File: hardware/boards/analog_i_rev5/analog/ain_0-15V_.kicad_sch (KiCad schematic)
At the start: 3 parts, among them IC22001 INA826AIDR

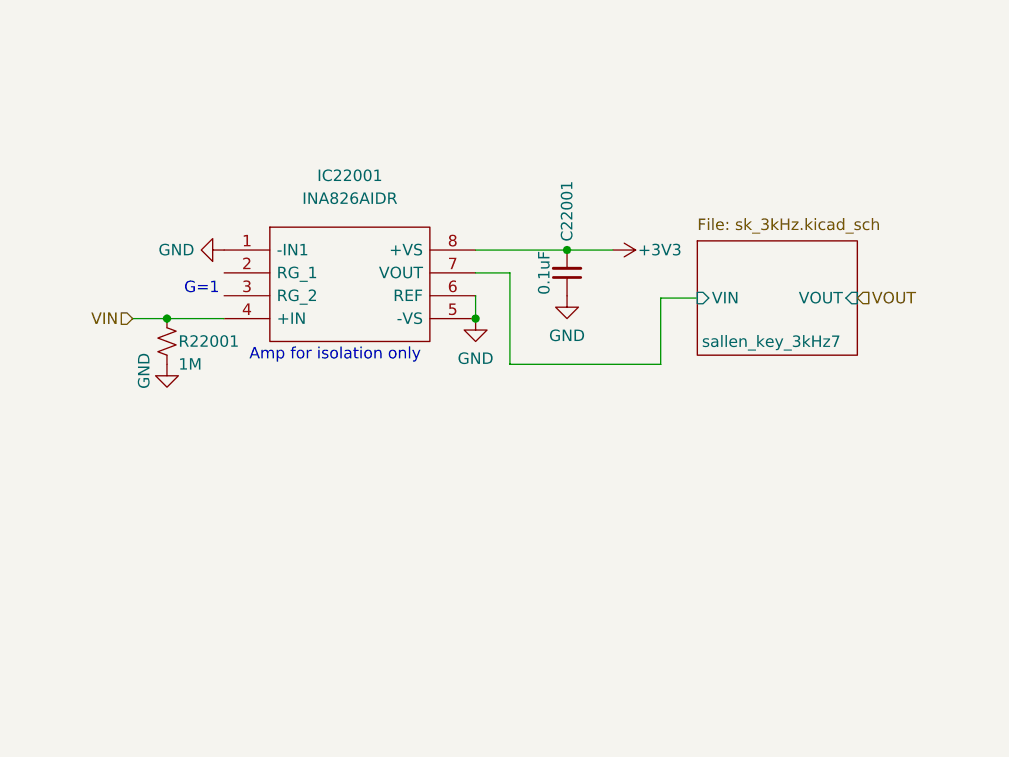
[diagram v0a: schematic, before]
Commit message: add 24V user power. make two voltage inputs 0-15V.
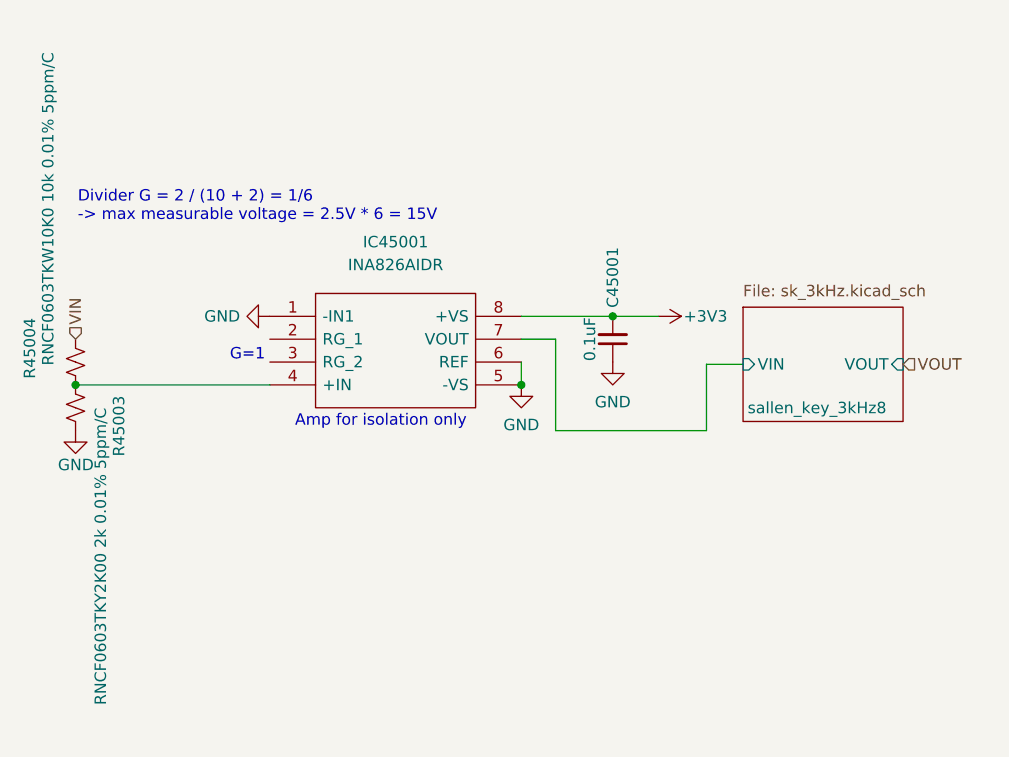
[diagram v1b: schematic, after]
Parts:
- removed C22001: 0.1uF, Capacitor_SMD:C_0402_1005Metric, symbol Device:C_Small
- removed IC22001: INA826AIDR, aaa:SOIC127P600X175-8N, symbol aaa:INA826AIDR
- removed R22001: 1M, Resistor_SMD:R_0402_1005Metric, symbol Device:R_Small_US
- added C45001: 0.1uF, Capacitor_SMD:C_0402_1005Metric, symbol Device:C_Small
- added IC45001: INA826AIDR, aaa:SOIC127P600X175-8N, symbol aaa:INA826AIDR
- added R45003: RNCF0603TKY2K00 2k 0.01% 5ppm/C, Resistor_SMD:R_0603_1608Metric, symbol Device:R_Small_US
- added R45004: RNCF0603TKW10K0 10k 0.01% 5ppm/C, Resistor_SMD:R_0603_1608Metric, symbol Device:R_Small_US
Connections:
- net +3V3: now also C45001.2, IC45001.8 (+VS)
- net GND: now also C45001.1, IC45001.1 (-IN1), IC45001.5 (-VS), IC45001.6 (REF), R45003.2
- net VIN: now also R45004.2
- new net: IC45001.4 (+IN), R45003.1, R45004.1
- new net sallen_key_3kHz8/VIN: IC45001.7 (VOUT)
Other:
- removed sheet sallen_key_3kHz7
- added sheet sallen_key_3kHz8 (sk_3kHz.kicad_sch)
- note added: "Divider G = 2 / (10 + 2) = 1/6 -> max measurable voltage = 2.5V * 6 = 15V"

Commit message: remove redundant esd diodes
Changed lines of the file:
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@@
 	(wire
 		(pts
-			(xy 155.448 109.728) (xy 138.684 109.728)
+			(xy 138.684 109.728) (xy 155.448 109.728)
 		)
 		(stroke

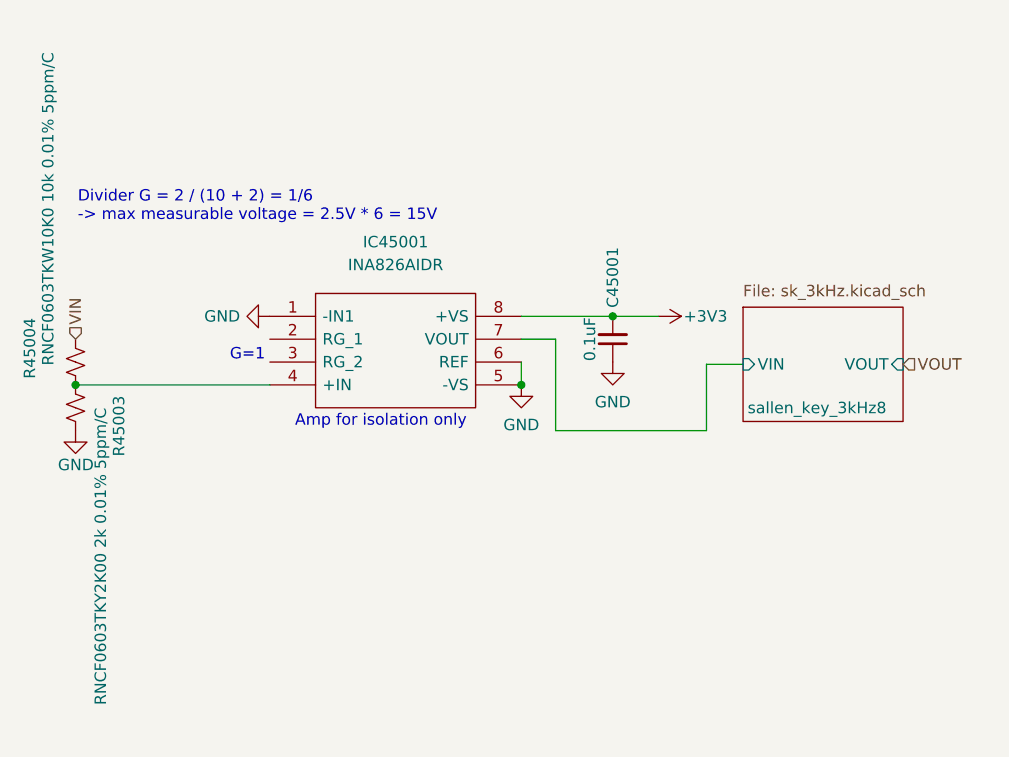
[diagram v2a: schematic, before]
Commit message: do layout for voltage inputs and dac/pwm outputs
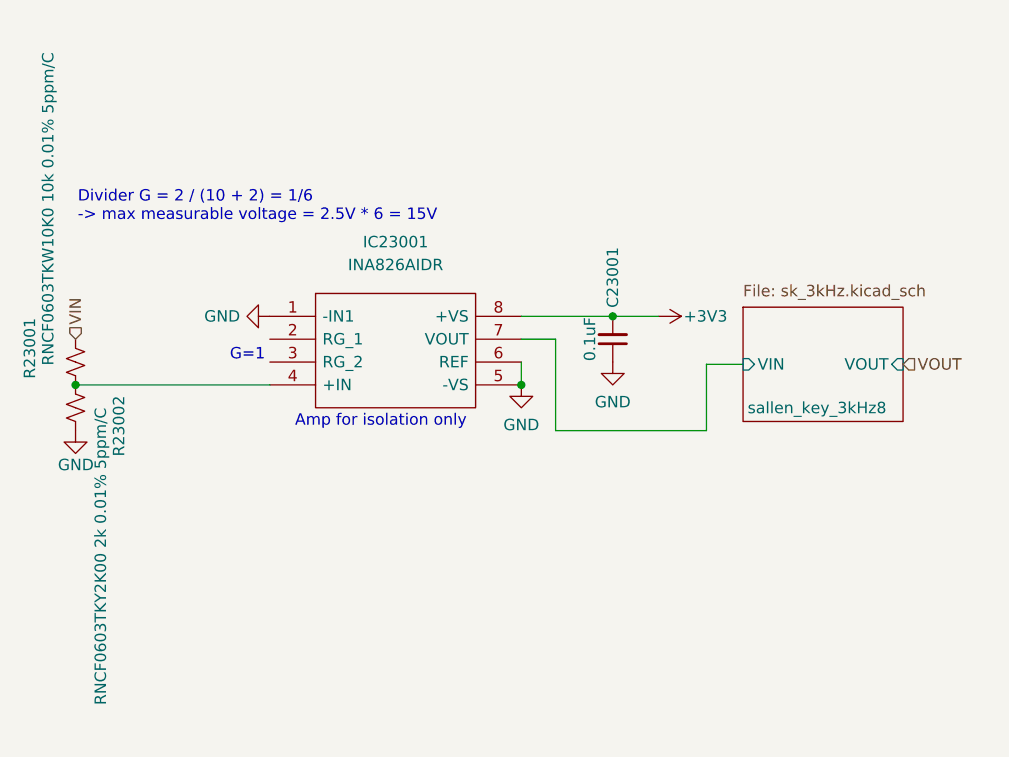
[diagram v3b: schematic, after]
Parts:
- renumbered C45001 to C23001, IC45001 to IC23001, R45004 to R23001, R45003 to R23002
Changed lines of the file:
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@@
 		(dnp no)
 		(fields_autoplaced yes)
-		(property "Reference" "IC45001"
+		(property "Reference" "IC23001"
 			(at 120.904 88.773 0)
 			(effects
@@
 		(on_board yes)
 		(dnp no)
-		(property "Reference" "R45003"
+		(property "Reference" "R23002"
 			(at 90.17 109.22 90)
 			(effects
@@
 		(on_board yes)
 		(dnp no)
-		(property "Reference" "#PWR45009"
+		(property "Reference" "#PWR23001"
 			(at 85.344 116.078 0)
 			(effects
@@
 		(on_board yes)
 		(dnp no)
-		(property "Reference" "#PWR45008"
+		(property "Reference" "#PWR23005"
 			(at 146.304 97.028 0)
 			(effects
@@
 		(on_board yes)
 		(dnp no)
-		(property "Reference" "R45004"
+		(property "Reference" "R23001"
 			(at 80.264 100.584 90)
 			(effects
@@
 		(dnp no)
 		(fields_autoplaced yes)
-		(property "Reference" "#PWR45005"
+		(property "Reference" "#PWR23002"
 			(at 100.584 97.028 0)
 			(effects
@@
 		(dnp no)
 		(fields_autoplaced yes)
-		(property "Reference" "#PWR45006"
+		(property "Reference" "#PWR23003"
 			(at 134.874 110.998 0)
 			(effects
@@
 		(on_board yes)
 		(dnp no)
-		(property "Reference" "C45001"
+		(property "Reference" "C23001"
 			(at 145.034 92.71 90)
 			(effects
@@
 		(dnp no)
 		(fields_autoplaced yes)
-		(property "Reference" "#PWR45007"
+		(property "Reference" "#PWR23004"
 			(at 145.034 108.458 0)
 			(effects

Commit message: shorten board and update combined layout
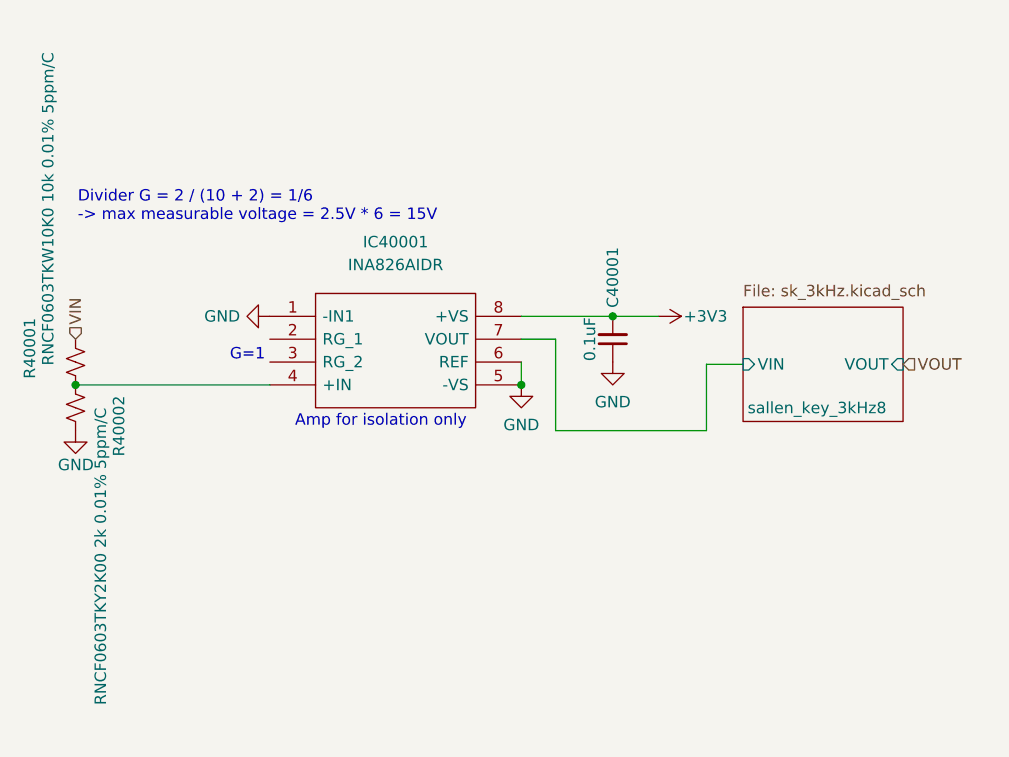
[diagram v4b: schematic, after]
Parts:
- renumbered C23001 to C40001, IC23001 to IC40001, R23001 to R40001, R23002 to R40002
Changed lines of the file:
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@@
 		(dnp no)
 		(fields_autoplaced yes)
-		(property "Reference" "IC23001"
+		(property "Reference" "IC40001"
 			(at 120.904 88.773 0)
 			(effects
@@
 		)
 		(instances
+			(project "analog_i"
+				(path "/5a60c4b1-b6cb-416e-8883-8291fa089b87/c2baf18d-2b19-4edb-98b3-535275ee271f/be220027-a1e7-4f8a-b4af-8d208623fd51"
+					(reference "IC40001")
+					(unit 1)
+				)
+				(path "/5a60c4b1-b6cb-416e-8883-8291fa089b87/c2baf18d-2b19-4edb-98b3-535275ee271f/ed2f7b43-1244-451f-9def-7c9639b384e1"
+					(reference "IC42001")
+					(unit 1)
+				)
+			)
 			(project "analog_frontend_panel"
 				(path "/c241d083-1323-4b4a-a540-956d0afb7b72/be220027-a1e7-4f8a-b4af-8d208623fd51"
@@
 		(on_board yes)
 		(dnp no)
-		(property "Reference" "R23002"
+		(property "Reference" "R40002"
 			(at 90.17 109.22 90)
 			(effects
@@
 		)
 		(instances
+			(project "analog_i"
+				(path "/5a60c4b1-b6cb-416e-8883-8291fa089b87/c2baf18d-2b19-4edb-98b3-535275ee271f/be220027-a1e7-4f8a-b4af-8d208623fd51"
+					(reference "R40002")
+					(unit 1)
+				)
+				(path "/5a60c4b1-b6cb-416e-8883-8291fa089b87/c2baf18d-2b19-4edb-98b3-535275ee271f/ed2f7b43-1244-451f-9def-7c9639b384e1"
+					(reference "R42002")
+					(unit 1)
+				)
+			)
 			(project "analog_frontend_panel"
 				(path "/c241d083-1323-4b4a-a540-956d0afb7b72/be220027-a1e7-4f8a-b4af-8d208623fd51"
@@
 		(on_board yes)
 		(dnp no)
-		(property "Reference" "#PWR23001"
+		(property "Reference" "#PWR231"
 			(at 85.344 116.078 0)
 			(effects
@@
 		)
 		(instances
+			(project "analog_i"
+				(path "/5a60c4b1-b6cb-416e-8883-8291fa089b87/c2baf18d-2b19-4edb-98b3-535275ee271f/be220027-a1e7-4f8a-b4af-8d208623fd51"
+					(reference "#PWR231")
+					(unit 1)
+				)
+				(path "/5a60c4b1-b6cb-416e-8883-8291fa089b87/c2baf18d-2b19-4edb-98b3-535275ee271f/ed2f7b43-1244-451f-9def-7c9639b384e1"
+					(reference "#PWR240")
+					(unit 1)
+				)
+			)
 			(project "analog_frontend_panel"
 				(path "/c241d083-1323-4b4a-a540-956d0afb7b72/be220027-a1e7-4f8a-b4af-8d208623fd51"
@@
 		(on_board yes)
 		(dnp no)
-		(property "Reference" "#PWR23005"
+		(property "Reference" "#PWR229"
 			(at 146.304 97.028 0)
 			(effects
@@
 		)
 		(instances
+			(project "analog_i"
+				(path "/5a60c4b1-b6cb-416e-8883-8291fa089b87/c2baf18d-2b19-4edb-98b3-535275ee271f/be220027-a1e7-4f8a-b4af-8d208623fd51"
+					(reference "#PWR229")
+					(unit 1)
+				)
+				(path "/5a60c4b1-b6cb-416e-8883-8291fa089b87/c2baf18d-2b19-4edb-98b3-535275ee271f/ed2f7b43-1244-451f-9def-7c9639b384e1"
+					(reference "#PWR238")
+					(unit 1)
+				)
+			)
 			(project "analog_frontend_panel"
 				(path "/c241d083-1323-4b4a-a540-956d0afb7b72/be220027-a1e7-4f8a-b4af-8d208623fd51"
@@
 		(on_board yes)
 		(dnp no)
-		(property "Reference" "R23001"
+		(property "Reference" "R40001"
 			(at 80.264 100.584 90)
 			(effects
@@
 		)
 		(instances
+			(project "analog_i"
+				(path "/5a60c4b1-b6cb-416e-8883-8291fa089b87/c2baf18d-2b19-4edb-98b3-535275ee271f/be220027-a1e7-4f8a-b4af-8d208623fd51"
+					(reference "R40001")
+					(unit 1)
+				)
+				(path "/5a60c4b1-b6cb-416e-8883-8291fa089b87/c2baf18d-2b19-4edb-98b3-535275ee271f/ed2f7b43-1244-451f-9def-7c9639b384e1"
+					(reference "R42001")
+					(unit 1)
+				)
+			)
 			(project "analog_frontend_panel"
 				(path "/c241d083-1323-4b4a-a540-956d0afb7b72/be220027-a1e7-4f8a-b4af-8d208623fd51"
@@
 		(dnp no)
 		(fields_autoplaced yes)
-		(property "Reference" "#PWR23002"
+		(property "Reference" "#PWR230"
 			(at 100.584 97.028 0)
 			(effects
@@
 		)
 		(instances
+			(project "analog_i"
+				(path "/5a60c4b1-b6cb-416e-8883-8291fa089b87/c2baf18d-2b19-4edb-98b3-535275ee271f/be220027-a1e7-4f8a-b4af-8d208623fd51"
+					(reference "#PWR230")
+					(unit 1)
+				)
+				(path "/5a60c4b1-b6cb-416e-8883-8291fa089b87/c2baf18d-2b19-4edb-98b3-535275ee271f/ed2f7b43-1244-451f-9def-7c9639b384e1"
+					(reference "#PWR239")
+					(unit 1)
+				)
+			)
 			(project "analog_frontend_panel"
 				(path "/c241d083-1323-4b4a-a540-956d0afb7b72/be220027-a1e7-4f8a-b4af-8d208623fd51"
@@
 		(dnp no)
 		(fields_autoplaced yes)
-		(property "Reference" "#PWR23003"
+		(property "Reference" "#PWR227"
 			(at 134.874 110.998 0)
 			(effects
@@
 		)
 		(instances
+			(project "analog_i"
+				(path "/5a60c4b1-b6cb-416e-8883-8291fa089b87/c2baf18d-2b19-4edb-98b3-535275ee271f/be220027-a1e7-4f8a-b4af-8d208623fd51"
+					(reference "#PWR227")
+					(unit 1)
+				)
+				(path "/5a60c4b1-b6cb-416e-8883-8291fa089b87/c2baf18d-2b19-4edb-98b3-535275ee271f/ed2f7b43-1244-451f-9def-7c9639b384e1"
+					(reference "#PWR236")
+					(unit 1)
+				)
+			)
 			(project "analog_frontend_panel"
 				(path "/c241d083-1323-4b4a-a540-956d0afb7b72/be220027-a1e7-4f8a-b4af-8d208623fd51"
@@
 		(on_board yes)
 		(dnp no)
-		(property "Reference" "C23001"
+		(property "Reference" "C40001"
 			(at 145.034 92.71 90)
 			(effects
@@
 		)
 		(instances
+			(project "analog_i"
+				(path "/5a60c4b1-b6cb-416e-8883-8291fa089b87/c2baf18d-2b19-4edb-98b3-535275ee271f/be220027-a1e7-4f8a-b4af-8d208623fd51"
+					(reference "C40001")
+					(unit 1)
+				)
+				(path "/5a60c4b1-b6cb-416e-8883-8291fa089b87/c2baf18d-2b19-4edb-98b3-535275ee271f/ed2f7b43-1244-451f-9def-7c9639b384e1"
+					(reference "C42001")
+					(unit 1)
+				)
+			)
 			(project "analog_frontend_panel"
 				(path "/c241d083-1323-4b4a-a540-956d0afb7b72/be220027-a1e7-4f8a-b4af-8d208623fd51"
@@
 		(dnp no)
 		(fields_autoplaced yes)
-		(property "Reference" "#PWR23004"
+		(property "Reference" "#PWR228"
 			(at 145.034 108.458 0)
 			(effects
@@
 		)
 		(instances
+			(project "analog_i"
+				(path "/5a60c4b1-b6cb-416e-8883-8291fa089b87/c2baf18d-2b19-4edb-98b3-535275ee271f/be220027-a1e7-4f8a-b4af-8d208623fd51"
+					(reference "#PWR228")
+					(unit 1)
+				)
+				(path "/5a60c4b1-b6cb-416e-8883-8291fa089b87/c2baf18d-2b19-4edb-98b3-535275ee271f/ed2f7b43-1244-451f-9def-7c9639b384e1"
+					(reference "#PWR237")
+					(unit 1)
+				)
+			)
 			(project "analog_frontend_panel"
 				(path "/c241d083-1323-4b4a-a540-956d0afb7b72/be220027-a1e7-4f8a-b4af-8d208623fd51"
